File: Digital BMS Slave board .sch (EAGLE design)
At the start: 91 parts, among them J1 S7B-PH-K

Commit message: Board size to chek
The schematic file is close to release ver.
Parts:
- removed C17: 1u/16V, resistor:C-EUC0603
- removed D6, D7, D8, D9: BAT60J, diode:BAT60J
- removed U$1: BQ79606A-Q1-HTQFP(PHP)|48, texas Instrumets:BQ79606A-Q1-HTQFP(PHP)|48
- removed U$2, U$3: S4B-PH-K, con-jst-ph:S4B-PH-K
- removed U$4, U$5: PESD2CAN, stmicroelectronics:PESD2CAN
- added C35, C36, C52, C53, C57: 51p, resistor:C-EUC0603
- added C50, C51, C54, C56: 2200p, resistor:C-EUC0603
- added C58, C59: 1nF, resistor:C-EUC0603
- added C60, C61, C62, C63, C64, C65, C66, C67, C68, C69, C70, C71, C74: 1u/16V, resistor:C-EUC0603
- added C72, C73, C75, C76: 1u/16V, Capacitors:C-EU-K-X0603
- added D1, D10, D11, D12, D2, D3: (no value), eagle-ltspice:DIODE_E-
- added J10, J9: S3B-PH-K, con-jst-ph:S3B-PH-K
- added J2, J3: S4B-PH-K, con-jst-ph:S4B-PH-K
- added J4: S6B-PH-K, con-jst-ph:S6B-PH-K
- added J5, J6, J7, J8: S2B-PH-K, con-jst-ph:S2B-PH-K
- added JP1: (no value), pinhead:PINHD-2X6
- added JP2: (no value), pinhead:PINHD-1X6
- added JP20: SOLDER_BRIDGE, testing:SOLDER_BRIDGE
- added JP3, JP4: (no value), pinhead:PINHD-1X7
- added JP5, JP6: (no value), pinhead:PINHD-2X7
- added L1, L2, L3, L4: 100uH, Inductors:TDK_ACT45BIND_BOURNS_SRF4532-M
- added Q1, Q2, Q3, Q4, Q5, Q6: BSS123, transistor-small-signal:BSS123
- added R100, R49, R52, R54, R56, R58, R60: 100, resistor:R-EU_R0603
- added R12, R13, R37, R38, R42, R43, R7, R8: 43, resistor:R-EU_R0603
- added R14, R39: 10k, resistor:R-EU_R0603
- added R15, R16, R40, R41: 10, resistor:R-EU_R0603
- added R44, R45, R46, R47: 100k, resistor:R-EU_R0603
- added R48, R51, R53, R55, R57, R59, R62, R65: 1k, resistor:R-EU_R0603
- added R50, R61, R63, R64, R66, R67: (no value), Resistors:R-EU0603
- added R68, R69, R70, R71, R72, R73: 10k, Resistors:R-EU0603
- added RB1, RB2, RB3, RB4, RB5, RB6: 20, resistor:R-EU_R0603
- added TP10, TP11, TP12, TP13, TP14, TP15, TP16, TP17, TP18, TP19, TP20, TP21, TP22, TP23, TP24, TP25, TP26, TP27, TP28, TP29, TP3, TP33, TP4, TP5, TP6, TP7, TP8, TP9: TEST_PAD2, testing:TEST_PAD2
- added TP30, TP31, TP32, TP34, TP35, TP36, TP37, TP38, TP39, TP40, TP41, TP42, TP43, TP44, TP45, TP46, TP47, TP48, TP49, TP50, TP51, TP52: TEST_PAD, testing:TEST_PAD
- added X1: BQ79606A-Q1-HTQFP(PHP)|48, texas Instrumets:BQ79606A-Q1-HTQFP(PHP)|48
- added X2, X3, X4, X5: PESD2CAN, stmicroelectronics:PESD2CAN
- C37, C38: value 51p -> 2200p
- C39, C49: value 2200p -> 51p
- D4, D5: value BAT60J -> 6.5V
- R10, R11, R4, R5: value 49 -> 10
- R20, R21: value 1k -> (none); device resistor:R-EU_R0603 -> Resistors:R-EU0603
- TP1: value TEST_PAD -> TEST_PAD2; device testing:TEST_PAD -> testing:TEST_PAD2
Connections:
- removed net N$28: C46.1, C47.1, C48.2, R35.2, U$1.CB1
- new net 123: JP6.12, R35.1
- new net 1234: JP6.14, R36.1
- new net AVDD: C6.1, X1.AVDD
- new net BAT1: C24.1, C25.2, J1.2, JP6.11, R28.1, TP1.P$1
- new net BAT105: JP6.6, R32.1
- new net BAT2: C23.1, C24.2, J1.3, JP6.9, R27.1, TP19.P$1
- new net BAT3: C22.1, C23.2, J1.4, JP6.7, R26.1, TP26.P$1
- new net BAT4: C21.1, C22.2, J1.5, JP6.5, R25.1, TP27.P$1
- new net BAT5: C20.1, C21.2, J1.6, JP6.3, R24.1, TP28.P$1
- new net BAT59: JP6.4, R31.1
- new net BAT65: JP6.8, R33.1
- new net BAT75: JP6.10, R34.1
- new net CB0: JP5.13, X1.CB0
- new net CB1: JP5.11, X1.CB1
- new net CB2: JP5.9, X1.CB2
- new net CB3: JP5.7, X1.CB3
- new net CB4: JP5.5, X1.CB4
- new net CB5: JP5.3, X1.CB5
- new net CB6: JP5.1, X1.CB6
- new net COMHN: C53.2, R39.1, R43.1, TP14.P$1, X1.COMHN
- new net COMHP: C52.2, R39.2, R42.1, TP13.P$1, X1.COMHP
- new net FAULTHN: C49.2, R14.1, R38.1, TP12.P$1, X1.FAULTHN
- new net FAULTHP: C39.2, R14.2, R37.1, TP11.P$1, X1.FAULTHP
- new net FAULTLN: C8.2, R3.1, R8.1, TP4.P$1, X1.FAULTLN
- new net FAULTLP: C5.2, R3.2, R7.1, TP3.P$1, X1.FAULTLP
- new net GPIO1: JP1.2, X1.GIPO1
- new net GPIO1V2: C14.2, D5.C, JP1.1, R17.1, TP51.P$1
- new net GPIO2: JP1.4, X1.GIPO2
- new net GPIO2V1: C15.2, D4.C, JP1.3, R18.1, TP52.P$1
- new net GPIO3: JP1.6, X1.GIPO3
- new net GPIO3T4: C74.2, JP1.5, R65.1, TP40.P$1
- new net GPIO4: JP1.12, X1.GIPO4
- new net GPIO4T3: C18.2, JP1.7, R62.1, TP38.P$1
- new net GPIO5: JP1.10, X1.GIPO5
- new net GPIO5T2: C19.2, JP1.9, R22.1, TP42.P$1
- new net GPIO6: JP1.8, X1.GIPO6
- new net GPIO6T1: C16.2, JP1.11, R19.1, TP43.P$1
- new net ISO_COMHN: J3.4, L4.3, TP17.P$1
- new net ISO_COMHP: J3.3, L4.4, TP18.P$1
- new net ISO_COMLN: J2.4, L2.3, TP7.P$1
- new net ISO_COMLP: J2.3, L2.4, TP8.P$1
- new net ISO_FAULTHN: J3.2, L3.3, TP16.P$1
- new net ISO_FAULTHP: J3.1, L3.4, TP15.P$1
- new net ISO_FAULTN: J2.2, L1.3, TP6.P$1
- new net ISO_FAULTP: J2.1, L1.4, TP5.P$1
- new net N$41: R5.1, R8.2, X2.2
- new net N$42: R4.1, R7.2, X2.1
- new net N$43: R11.1, R13.2, X5.2
- new net N$44: R10.1, R12.2, X5.1
- new net N$45: C38.1, L2.1
- new net N$46: C37.1, L2.2
- new net N$47: C50.2, R16.2
- new net N$48: C51.2, R15.2
- new net N$53: C54.2, R41.2
- new net N$54: C56.2, R40.2
- new net N$55: R41.1, R43.2, X4.2
- new net N$56: R40.1, R42.2, X4.1
- new net N$57: C56.1, L4.1
- new net N$58: C54.1, L4.2
- new net N$60: C63.2, D2.A, Q2.G, R51.1
- new net N$61: C62.1, C64.2, JP4.3, R51.2, R52.2
- new net N$62: C65.2, D3.A, Q3.G, R53.1
- new net N$63: Q4.D, RB4.1
- new net N$64: C65.1, D3.C, JP3.4, Q3.S, R54.1, RB4.2
- new net N$65: C64.1, C66.2, JP4.4, R53.2, R54.2
- new net N$66: C66.1, C68.2, JP4.5, R55.2, R56.2
- new net N$67: C67.1, D10.C, JP3.5, Q4.S, R56.1, RB5.2
- new net N$68: C67.2, D10.A, Q4.G, R55.1
- new net N$69: C44.1, C45.2, JP5.8, R33.2
- new net N$70: C69.2, D11.A, Q5.G, R57.1
- new net N$71: Q6.D, RB6.1
- new net N$72: C69.1, D11.C, JP3.6, Q5.S, R58.1, RB6.2
- new net N$73: C68.1, C70.2, JP4.6, R57.2, R58.2
- new net N$74: C70.1, JP4.7, R59.2, R60.2
- new net N$75: C71.1, D12.C, JP3.7, Q6.S, R60.1
- new net N$76: C71.2, D12.A, Q6.G, R59.1
- new net N$77: C48.1, C55.2, JP5.14, R36.2
- new net N$78: C41.2, JP5.2, R30.2
- new net N$79: C46.1, C47.1, C48.2, JP5.12, R35.2
- new net N$80: C45.1, C46.2, C47.2, JP5.10, R34.2
- new net N$81: C42.1, C43.1, C44.2, JP5.6, R32.2
- new net N$83: C31.1, C32.1, C33.2, R28.2, TP2.P$1, X1.VC1
- new net NFAULT: C59.2, J4.5, R45.1, TP35.P$1, X1.NFAULT
- new net REF1: C4.1, X1.REF1
- new net RX: C57.2, J4.3, R47.1, TP32.P$1, X1.RX
- new net TSREF: C3.1, C72.1, C73.1, C75.1, C76.1, J10.1, J9.1, R20.2, R50.2, R63.2, R66.2, TP45.P$1, TP48.P$1, X1.TSREF
- new net TX: J4.2, TP31.P$1, X1.TX
- new net VCC15: JP6.2, R30.1
- new net VIO: C11.1, C7.1, C9.1, J4.1, R45.2, R46.2, R47.2, TP30.P$1, X1.CVDD, X1.VIO, X1.VLDO
- new net WAKEUP: C58.2, J4.4, JP20.2, R46.1, TP34.P$1, X1.WAKEUP
- net COMLN: now also C36.2, R13.1, TP10.P$1, X1.COMLN; no longer C38.1, R11.1, U$1.COMLN
- net COMLP: now also C35.2, R12.1, TP9.P$1, X1.COMLP; no longer C37.2, R10.1, U$1.COMLP
- net GND: now also C25.1, C35.1, C36.1, C39.1, C49.1, C52.1, C53.1, C57.1, C58.1, C59.1, C72.2, C73.2, C74.1, C75.2, C76.2, C8.1, J10.3, J4.6, J5.2, J6.2, J7.2, J8.2, J9.3, JP20.1, JP6.13, R21.1, R29.1, R61.1, R64.1, R67.1, R68.2, R69.2, R70.2, R71.2, R72.2, R73.2, TP33.P$1, TP36.P$1, TP47.P$1, TP50.P$1, X1.AVSS@0, X1.AVSS@1, X1.CVSS, X1.DVSS, X2.3, X3.3, X4.3, X5.3; no longer C17.1, C37.1, C38.2, C8.2, D6.A, D7.A, D8.A, D9.A, U$1.AVSS@0, U$1.AVSS@1, U$1.CVSS, U$1.DVSS
- net N$1: now also X1.BAT; no longer U$1.BAT
- net N$10: now also J6.1, R62.2, R63.1, R64.2, TP37.P$1; no longer C22.1, C23.2, J1.4, R26.1, R33.1
- net N$11: now also J7.1, R65.2, R66.1, R67.2, TP39.P$1; no longer C23.1, C24.2, J1.3, R27.1, R34.1
- net N$12: now also JP2.1, R73.1; no longer C24.1, C25.2, J1.2, R28.1, R35.1, TP1.P$1
- net N$13: now also TP24.P$1, X1.VC5; no longer U$1.VC5
- net N$14: now also C41.1, C42.2, C43.2, JP5.4, R31.2; no longer C27.1, C28.1, C29.2, R25.2, U$1.VC4
- net N$15: now also TP22.P$1, X1.VC3; no longer U$1.VC3
- net N$16: now also TP21.P$1, X1.VC2; no longer U$1.VC2
- net N$17: now also C27.1, C28.1, C29.2, R25.2, TP23.P$1, X1.VC4; no longer C31.1, C32.1, C33.2, R28.2, TP2.P$1, U$1.VC1
- net N$18: now also TP20.P$1, X1.VC0; no longer U$1.VC0
- net N$19: now also JP2.2, R72.1; no longer C42.1, C43.1, C44.2, R32.2, U$1.CB4
- net N$2: now also X1.LDOIN; no longer U$1.LDOIN
- net N$20: now also JP2.3, R71.1; no longer C44.1, C45.2, R33.2, U$1.CB3
- net N$21: now also JP2.4, R70.1; no longer C45.1, C46.2, C47.2, R34.2, U$1.CB2
- net N$22: now also Q3.D, RB3.1; no longer C3.1, U$1.TSREF
- net N$23: now also JP2.5, R69.1; no longer C48.1, C55.2, R36.2, U$1.CB0
- net N$24: now also JP2.6, R68.1; no longer C41.1, C42.2, C43.2, R31.2, U$1.CB5
- net N$25: now also J10.2, R17.2, TP46.P$1; no longer C25.1, R29.1, R36.1
- net N$26: now also TP25.P$1, X1.VC6; no longer U$1.VC6
- net N$27: now also J9.2, R18.2, TP49.P$1; no longer C20.1, C21.2, J1.6, R24.1, R31.1
- net N$29: now also C63.1, D2.C, JP3.3, Q2.S, R52.1, RB3.2; no longer C14.2, D9.C, R17.1, U$1.GIPO1
- net N$3: now also Q1.D, RB1.1; no longer C11.1, C7.1, C9.1, U$1.CVDD, U$1.VIO, U$1.VLDO
- net N$30: now also C61.2, D1.A, Q1.G, R48.1; no longer C19.2, D4.C, R22.1, U$1.GIPO6
- net N$31: now also Q2.D, RB2.1; no longer C18.2, D5.C, R21.1, U$1.GIPO5
- net N$32: now also C61.1, D1.C, JP3.2, Q1.S, R49.1, RB2.2; no longer C17.2, D6.C, R20.1, U$1.GIPO4
- net N$33: now also C60.1, C62.2, JP4.2, R48.2, R49.2; no longer C16.2, D7.C, R19.1, U$1.GIPO3
- net N$34: now also Q5.D, RB5.1; no longer C15.2, D8.C, R18.1, U$1.GIPO2
- net N$35: now also C37.2, R11.2; no longer C5.2, R3.2, R4.1, U$1.FAULTLP
- net N$36: now also C38.2, R10.2; no longer C8.1, R3.1, R5.1, U$1.FAULTLN
- net N$39: now also L1.1; no longer U$2.1
- net N$4: now also JP3.1, R100.1, RB1.2; no longer C6.1, U$1.AVDD
- net N$40: now also L1.2; no longer U$2.2
- net N$49: now also R16.1, R38.2, X3.2; no longer C39.2, R11.2
- net N$5: now also X1.DVDD; no longer U$1.DVDD
- net N$50: now also R15.1, R37.2, X3.1; no longer C49.2, R10.2
- net N$51: now also C51.1, L3.1; no longer C49.1, U$2.3
- net N$52: now also C50.1, L3.2; no longer C39.1, U$2.4
- net N$6: now also C60.2, JP4.1, R100.2; no longer C4.1, U$1.REF1
- net N$7: now also X1.VPROG; no longer U$1.VPROG
- net N$8: now also J8.1, R22.2, R50.1, R61.2, TP41.P$1; no longer C41.2, R30.2, U$1.CB6
- net N$9: now also J5.1, R19.2, R20.1, R21.2, TP44.P$1; no longer C21.1, C22.2, J1.5, R25.1, R32.1
- net VCC: now also JP6.1, TP29.P$1; no longer R30.1
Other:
- note added: "10 kΩ - 100 kΩ RX pull up resistor nominal value"
- note added: "CAP+Choke configuration used for different PCB with less than 2m wiring"
- note added: "For stacked devices WAKEUP should be tied to AVSS. RX pulled up NFAULT and TX left unconnected"
- note added: "remeber about TX pull up resistor on the other side (isolator board)"
- note removed: "different PCB with less than 2m wiring"
- note removed: "same PCB config."

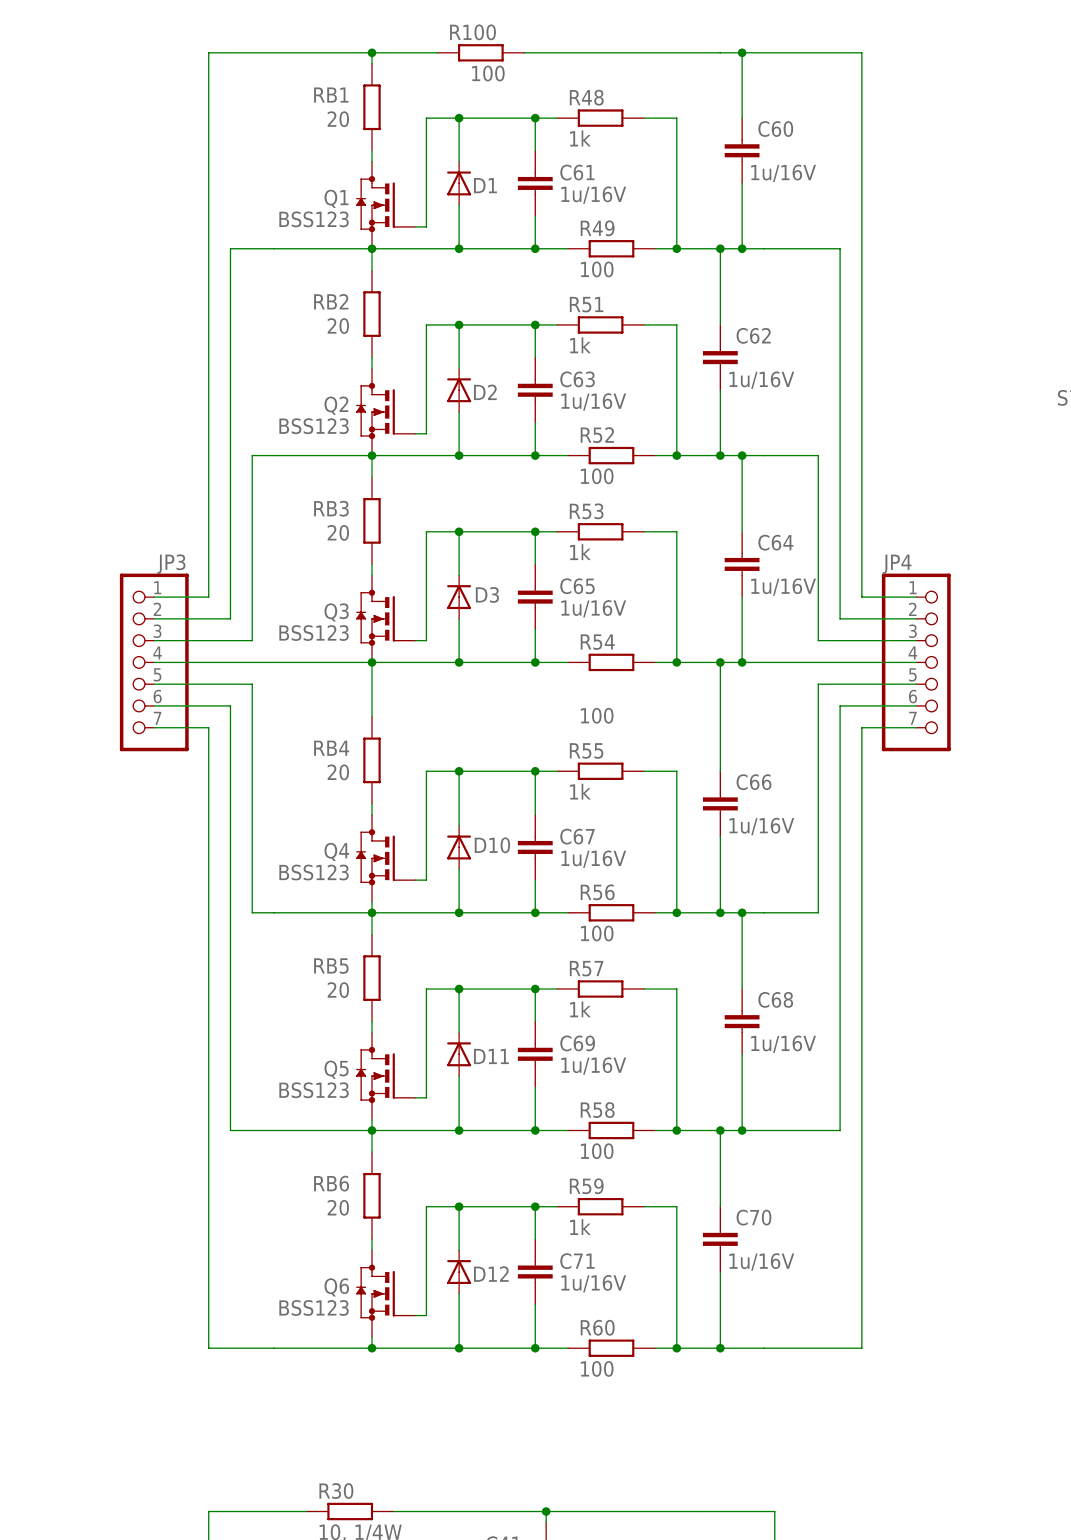
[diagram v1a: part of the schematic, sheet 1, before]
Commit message: 3d models fixed
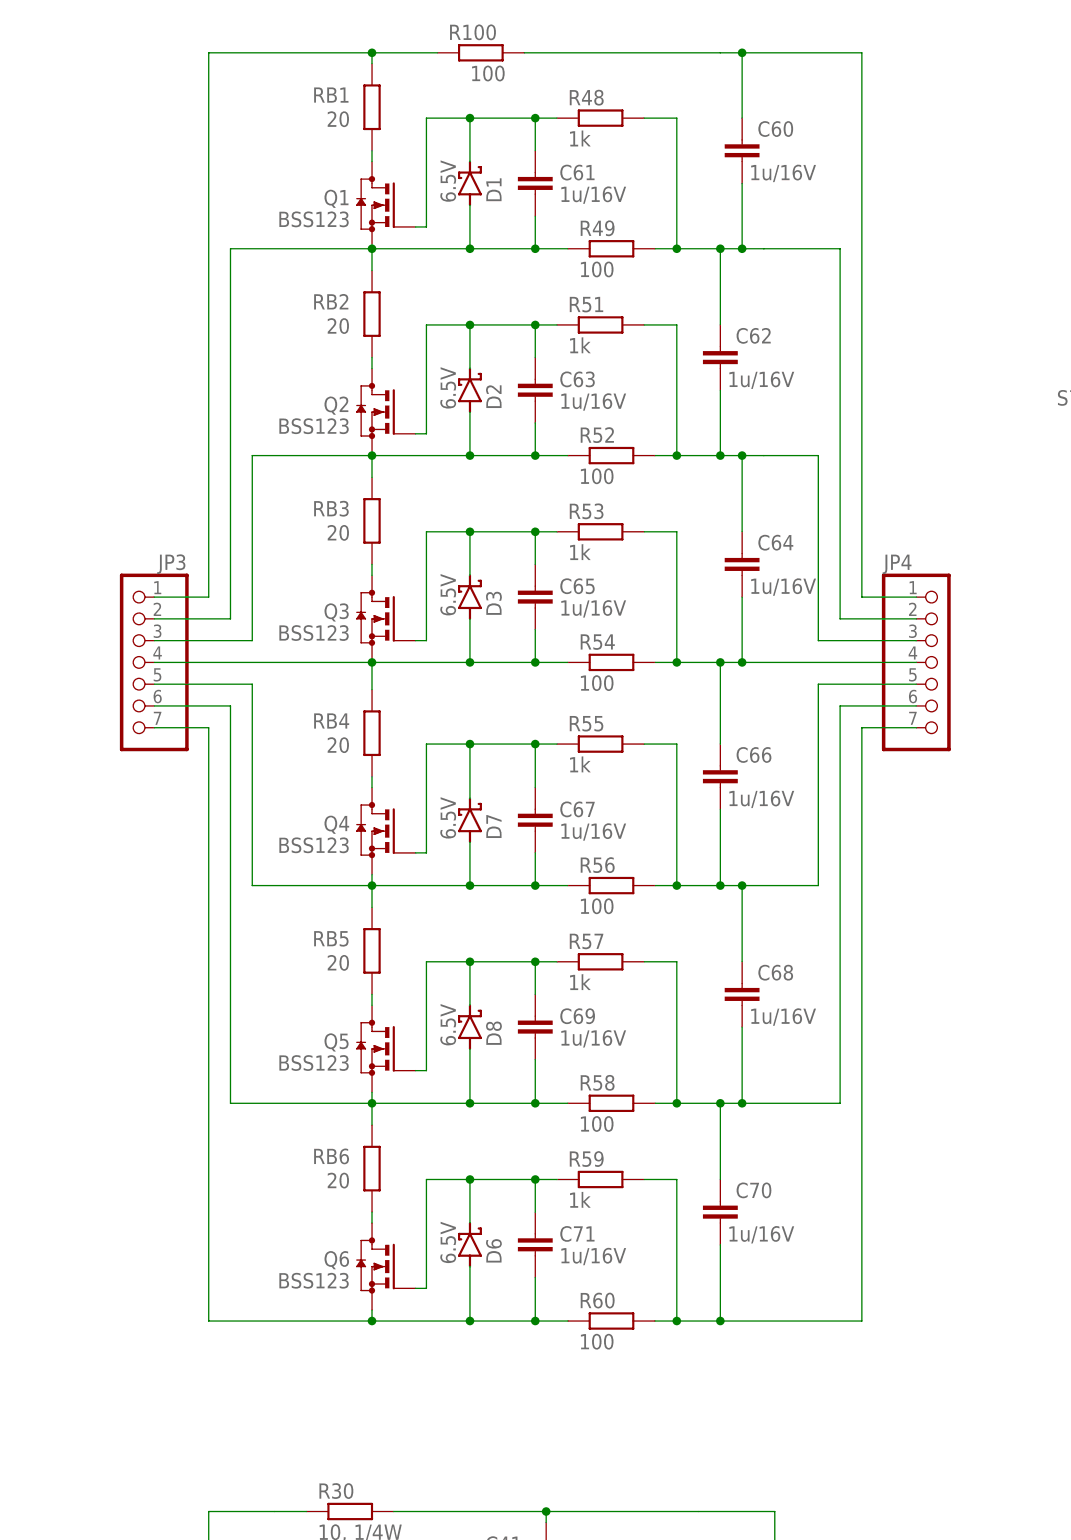
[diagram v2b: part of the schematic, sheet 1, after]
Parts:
- removed D10, D11, D12: (no value), eagle-ltspice:DIODE_E-
- added D6, D7, D8: 6.5V, Semiconductor_devices:SOD323-ZENER
- D1, D2, D3: value (none) -> 6.5V; device eagle-ltspice:DIODE_E- -> Semiconductor_devices:SOD323-ZENER
- D4, D5: device diode:BAT60J -> Semiconductor_devices:SOD323-ZENER
- J1: device con-jst-ph:B7B-PH-K -> con-jst-ph:S7B-PH-K
- JP2: device pinhead:PINHD-1X6 -> commonly used connectors:PINHD-1X6-OCT
- JP3, JP4: device pinhead:PINHD-1X7 -> commonly used connectors:PINHD-1X7-OCT
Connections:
- net N$29: now also D2.A; no longer D2.C
- net N$30: now also D1.C; no longer D1.A
- net N$32: now also D1.A; no longer D1.C
- net N$60: now also D2.C; no longer D2.A
- net N$62: now also D3.C; no longer D3.A
- net N$64: now also D3.A; no longer D3.C
- net N$67: now also D7.A; no longer D10.C
- net N$68: now also D7.C; no longer D10.A
- net N$70: now also D8.C; no longer D11.A
- net N$72: now also D8.A; no longer D11.C
- net N$75: now also D6.A; no longer D12.C
- net N$76: now also D6.C; no longer D12.A
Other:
- moved on the sheet: C66, C67, C68, C69, C70, C71, Q4, Q5, Q6, R55, R56, R57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
